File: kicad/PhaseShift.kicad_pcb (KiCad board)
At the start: 2 copper layers, 66.4 x 128.6 mm, 39 parts

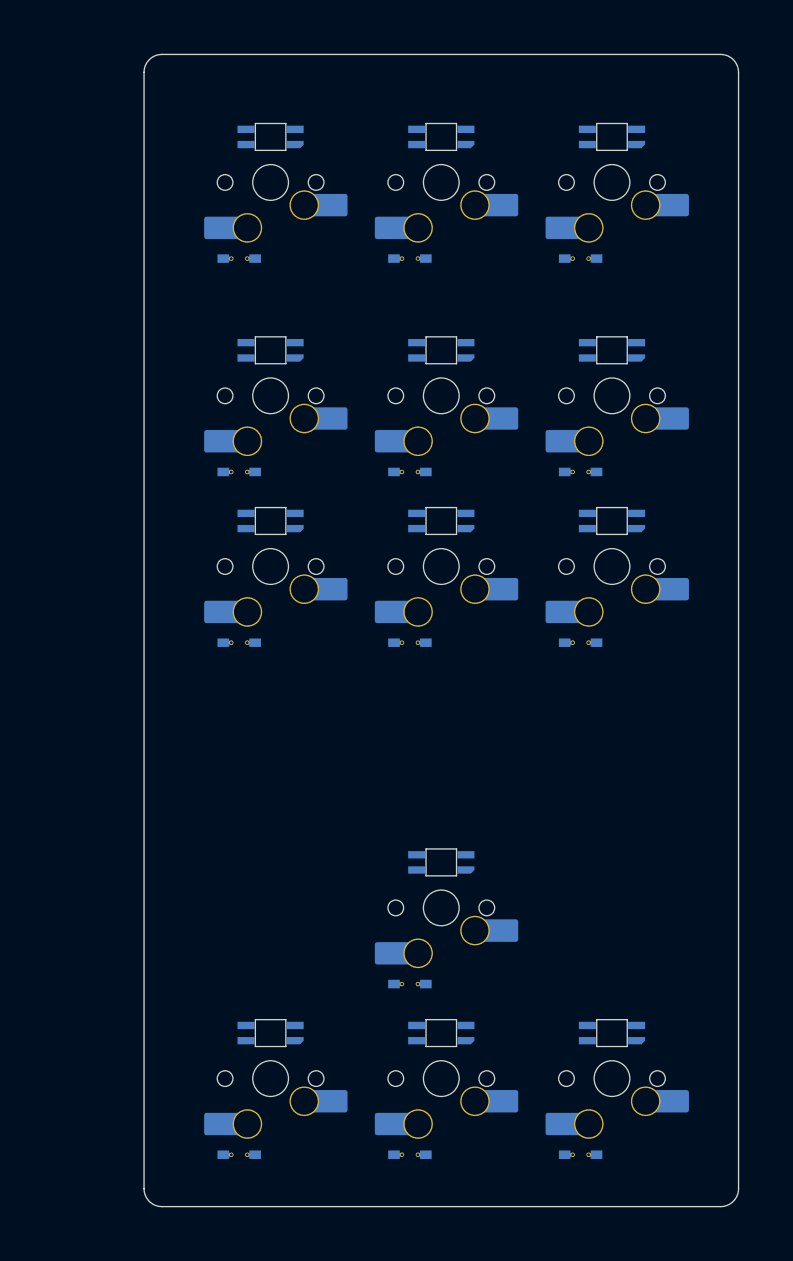
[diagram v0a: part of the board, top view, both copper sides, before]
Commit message: added MCU
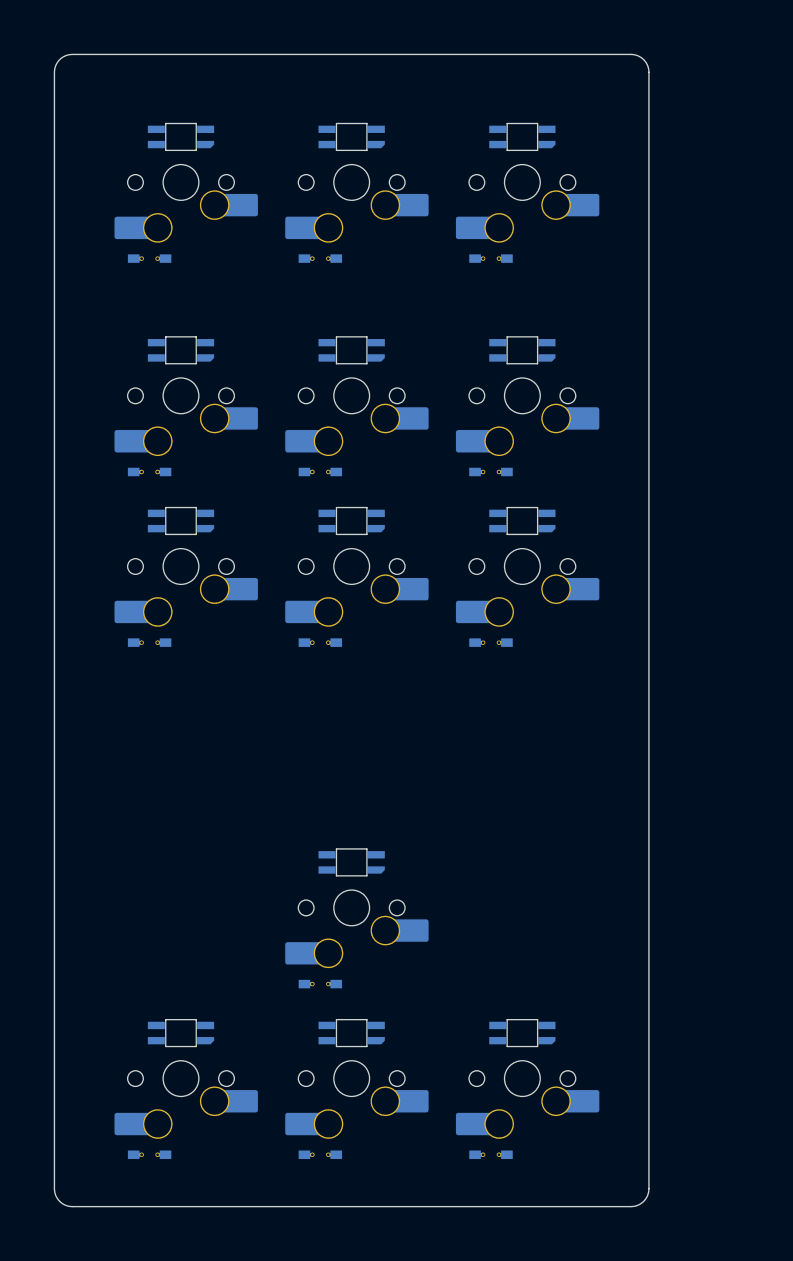
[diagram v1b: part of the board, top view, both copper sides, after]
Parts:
- moved D1 10.0 mm to (161.9, 98.5)
- moved D10 10.0 mm to (181.0, 179.5)
- moved D11 10.0 mm to (161.9, 198.5)
- moved D12 10.0 mm to (181.0, 198.5)
- moved D13 10.0 mm to (200.1, 198.5)
- moved D2 10.0 mm to (161.9, 122.3)
- moved D3 10.0 mm to (161.9, 141.4)
- moved D4 10.0 mm to (181.0, 98.5)
- moved D5 10.0 mm to (181.0, 122.3)
- moved D6 10.0 mm to (181.0, 141.4)
- moved D7 10.0 mm to (200.1, 98.5)
- moved D8 10.0 mm to (200.1, 122.3)
- moved D9 10.0 mm to (200.1, 141.4)
- moved L1 10.0 mm to (165.4, 84.9)
- moved L10 10.0 mm to (184.5, 165.9)
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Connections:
- S1 pad 1: col_0 -> Net-(D1-A)
- S1 pad 2: Net-(D1-A) -> col_0
- S10 pad 1: col_1 -> Net-(D10-A)
- S10 pad 2: Net-(D10-A) -> col_1
- S11 pad 1: col_0 -> Net-(D11-A)
- S11 pad 2: Net-(D11-A) -> col_0
- S12 pad 1: col_1 -> Net-(D12-A)
- S12 pad 2: Net-(D12-A) -> col_1
- S13 pad 1: col_2 -> Net-(D13-A)
- S13 pad 2: Net-(D13-A) -> col_2
- S2 pad 1: col_0 -> Net-(D2-A)
- S2 pad 2: Net-(D2-A) -> col_0
- S3 pad 1: col_0 -> Net-(D3-A)
- S3 pad 2: Net-(D3-A) -> col_0
- S4 pad 1: col_1 -> Net-(D4-A)
- S4 pad 2: Net-(D4-A) -> col_1
- S5 pad 1: col_1 -> Net-(D5-A)
- S5 pad 2: Net-(D5-A) -> col_1
- S6 pad 1: col_1 -> Net-(D6-A)
- S6 pad 2: Net-(D6-A) -> col_1
- S7 pad 1: col_2 -> Net-(D7-A)
- S7 pad 2: Net-(D7-A) -> col_2
- S8 pad 1: col_2 -> Net-(D8-A)
- S8 pad 2: Net-(D8-A) -> col_2
- S9 pad 1: col_2 -> Net-(D9-A)
- S9 pad 2: Net-(D9-A) -> col_2

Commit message: updated MCU
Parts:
- D1, D10, D11, D12, D13, D2, D3, D4, D5, D6, D7, D8, D9: value 1N4148W -> (none)
- S1, S10, S11, S12, S2, S3, S4, S5, S6, S7, S8, S9: value SW_MX_HS -> (none)
- S13: value SW_MX_HS_1u -> (none)
- moved D1 210.0 mm to (372.0, 98.5)
- moved D10 210.0 mm to (391.0, 179.5)
- moved D11 210.0 mm to (372.0, 198.5)
- moved D12 210.0 mm to (391.0, 198.5)
- moved D13 210.0 mm to (410.1, 198.5)
- moved D2 210.0 mm to (372.0, 122.3)
- moved D3 210.0 mm to (372.0, 141.4)
- moved D4 210.0 mm to (391.0, 98.5)
- moved D5 210.0 mm to (391.0, 122.3)
- moved D6 210.0 mm to (391.0, 141.4)
- moved D7 210.0 mm to (410.1, 98.5)
- moved D8 210.0 mm to (410.1, 122.3)
- moved D9 210.0 mm to (410.1, 141.4)
- moved L1 210.0 mm to (375.5, 84.9)
- moved L10 210.0 mm to (394.5, 165.9)
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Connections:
- net Net-(D1-A) renamed c14_func
- net Net-(D10-A) renamed c15_bottom
- net Net-(D11-A) renamed c14_thumb
- net Net-(D12-A) renamed c15_thumb
- net Net-(D13-A) renamed c16_thumb
- net Net-(D2-A) renamed c14_number
- net Net-(D3-A) renamed c14_top
- net Net-(D4-A) renamed c15_func
- net Net-(D5-A) renamed c15_number
- net Net-(D6-A) renamed c15_top
- net Net-(D7-A) renamed c16_func
- net Net-(D8-A) renamed c16_number
- net Net-(D9-A) renamed c16_top
- net col_2 renamed col_3
- net row_12 renamed function
- net row_13 renamed number
- net row_14 renamed top
- net row_16 renamed bottom
- net row_17 renamed thumb
- S1 pad 2: col_0 -> col_1
- S10 pad 2: col_1 -> col_4
- S11 pad 2: col_0 -> col_1
- S12 pad 2: col_1 -> col_4
- S2 pad 2: col_0 -> col_1
- S3 pad 2: col_0 -> col_1
- S4 pad 2: col_1 -> col_4
- S5 pad 2: col_1 -> col_4
- S6 pad 2: col_1 -> col_4

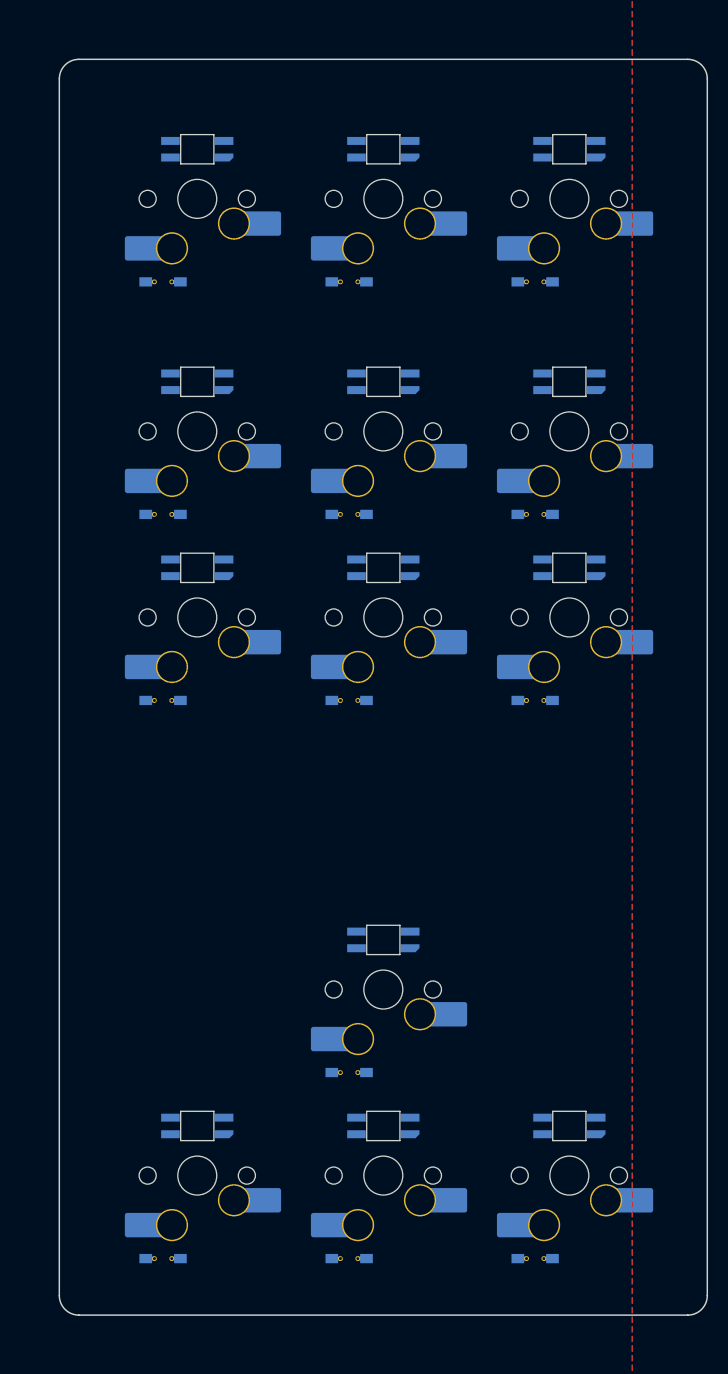
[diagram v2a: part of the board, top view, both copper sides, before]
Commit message: screw holes
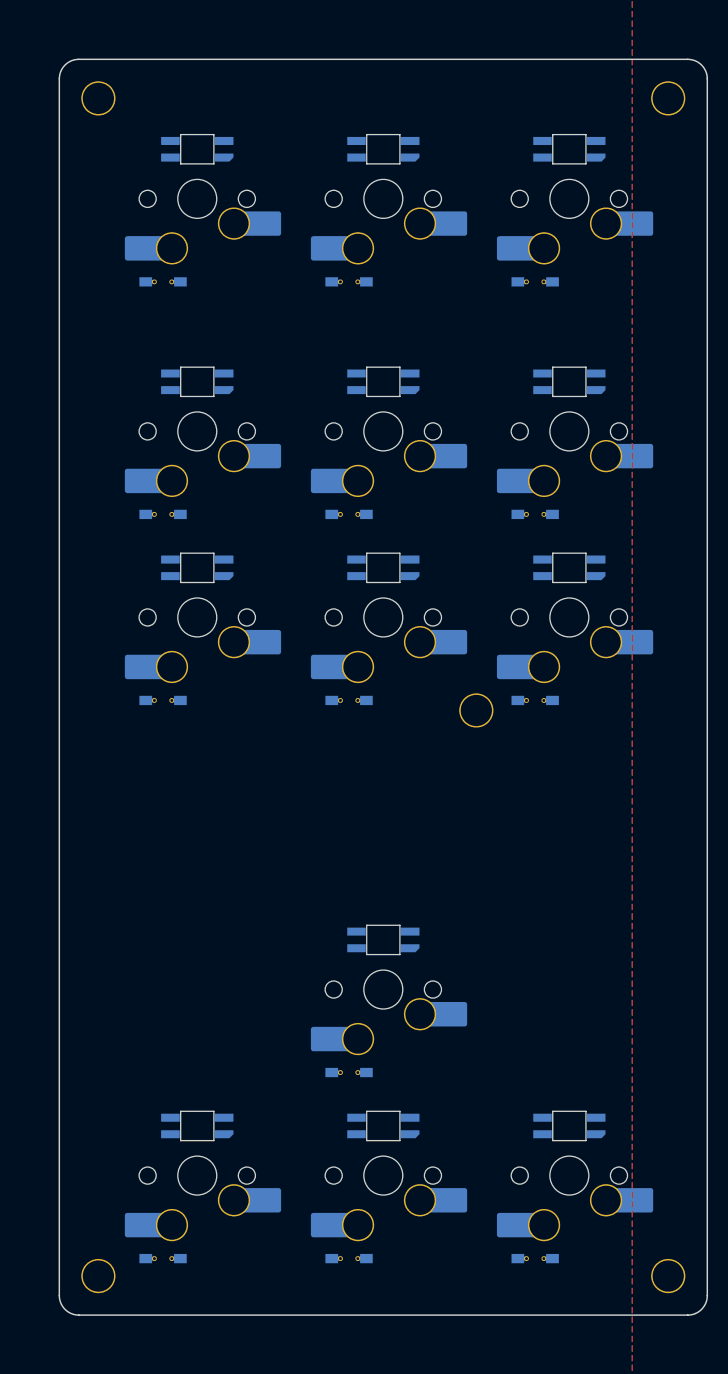
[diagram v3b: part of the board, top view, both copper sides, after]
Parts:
- added H1: MountingHole_3.2mm_Pad, TB2086_MISC:MountingHole_3.2mm_Pad, F.Cu at (365.3, 79.7)
- added H2: MountingHole_3.2mm_Pad, TB2086_MISC:MountingHole_3.2mm_Pad, F.Cu at (423.7, 79.7)
- added H3: MountingHole_3.2mm_Pad, TB2086_MISC:MountingHole_3.2mm_Pad, F.Cu at (423.7, 200.3)
- added H4: MountingHole_3.2mm_Pad, TB2086_MISC:MountingHole_3.2mm_Pad, F.Cu at (365.3, 200.3)
- added H5: MountingHole_3.2mm_Pad, TB2086_MISC:MountingHole_3.2mm_Pad, F.Cu at (404.0, 142.4)

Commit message: pogo pin - ergogen
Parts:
- added POGO1: Pogopin_1x05_P2.54mm_Curved, TB2086_MISC:Pogopin_1x05_P2.54mm_Curved, B.Cu at (175.4, 95.5)
- added POGO2: Pogopin_1x05_P2.54mm_Curved, TB2086_MISC:Pogopin_1x05_P2.54mm_Curved, B.Cu at (233.6, 95.5)
- added POGO3: Pogopin_1x07_P2.54mm_Curved, TB2086_MISC:Pogopin_1x07_P2.54mm_Curved, B.Cu at (175.4, 142.4)
- added POGO4: Pogopin_1x07_P2.54mm_Curved, TB2086_MISC:Pogopin_1x07_P2.54mm_Curved, B.Cu at (233.6, 142.4)
- added POGO5: Pogopin_1x07_P2.54mm_Curved, TB2086_MISC:Pogopin_1x07_P2.54mm_Curved, B.Cu at (175.4, 182.0)
- added POGO6: Pogopin_1x07_P2.54mm_Curved, TB2086_MISC:Pogopin_1x07_P2.54mm_Curved, B.Cu at (233.6, 182.0)
- moved D1 190.0 mm to (181.9, 98.5)
- moved D10 190.0 mm to (201.0, 179.5)
- moved D11 190.0 mm to (181.9, 198.5)
- moved D12 190.0 mm to (201.0, 198.5)
- moved D13 190.0 mm to (220.1, 198.5)
- moved D2 190.0 mm to (181.9, 122.3)
- moved D3 190.0 mm to (181.9, 141.4)
- moved D4 190.0 mm to (201.0, 98.5)
- moved D5 190.0 mm to (201.0, 122.3)
- moved D6 190.0 mm to (201.0, 141.4)
- moved D7 190.0 mm to (220.1, 98.5)
- moved D8 190.0 mm to (220.1, 122.3)
- moved D9 190.0 mm to (220.1, 141.4)
- moved H1 190.0 mm to (175.3, 79.7)
- moved H2 190.0 mm to (233.7, 79.7)
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
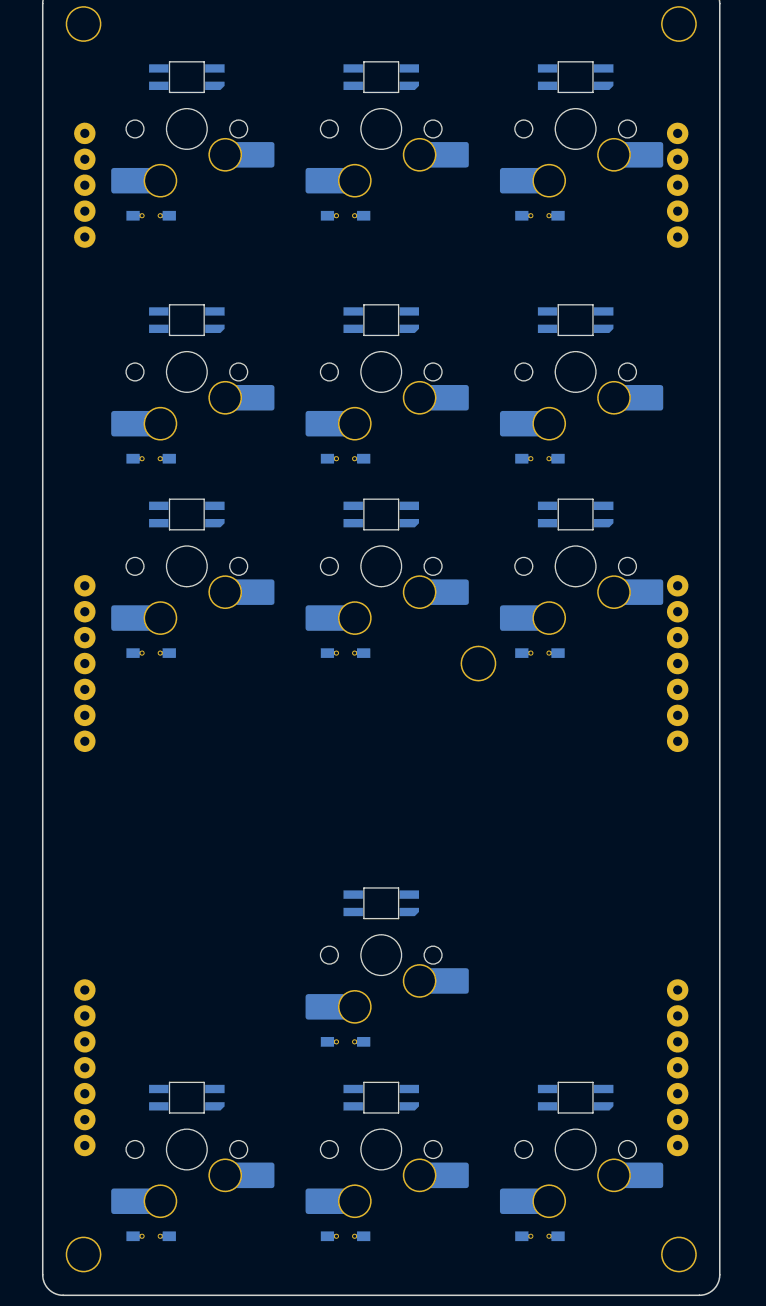
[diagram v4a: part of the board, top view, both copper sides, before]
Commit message: artwork for PhaseShift
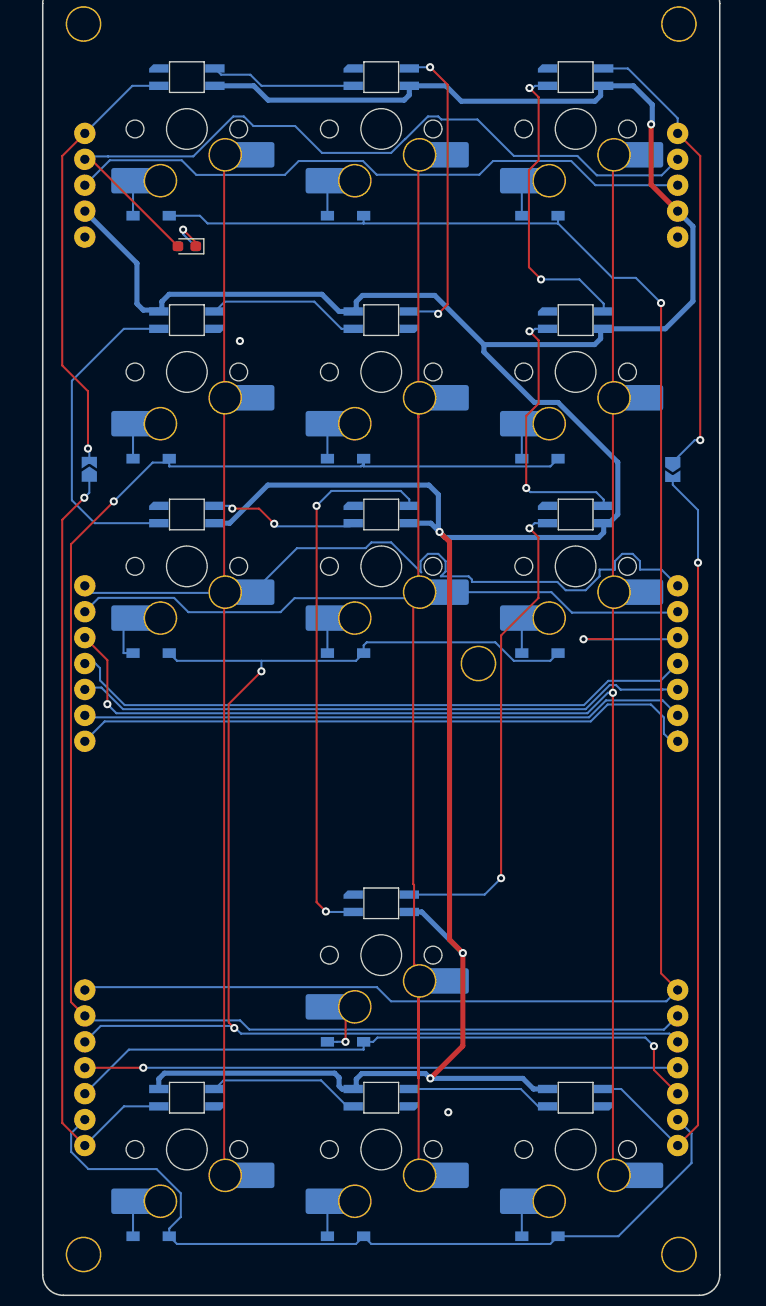
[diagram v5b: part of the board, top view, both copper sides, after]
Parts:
- added JP1: SolderJumper_2_Open, TB2086_MISC:SolderJumper-2_P1.3mm_Open_TrianglePad1.0x1.5mm, B.Cu at (175.9, 123.3)
- added JP2: SolderJumper_2_Open, TB2086_MISC:SolderJumper-2_P1.3mm_Open_TrianglePad1.0x1.5mm, B.Cu at (233.1, 123.4)
- added LED1: GREEN, LED_SMD:LED_0603_1608Metric_Pad1.05x0.95mm_HandSolder, F.Cu at (185.4, 101.5)
- added R1: 330, Resistor_SMD:R_0603_1608Metric, B.Cu at (185.4, 101.5)
- D1, D10, D11, D12, D13, D2, D3, D4, D5, D6, D7, D8, D9: value (none) -> 1N4148W
- L1, L10, L11, L12, L13, L2, L3, L4, L5, L6, L7, L8, L9: value TB2086_LED:LED_SK6812MINI-E -> SK6812MINI-E; footprint TB2086_LED:LED_SK6812MINI-E -> TB2086_LED_G:LED_SK6812MINI-E
- POGO1, POGO2: value Pogopin_1x05_P2.54mm_Curved -> Conn_01x05
- POGO3, POGO4, POGO5, POGO6: value Pogopin_1x07_P2.54mm_Curved -> Conn_01x07
- S1, S10, S11, S12, S2, S3, S4, S5, S6, S7, S8, S9: value (none) -> SW_MX_HS
- S13: value (none) -> SW_MX_HS_1u
- turned L1 to 180 degrees
- turned L10 to 180 degrees
- turned L3 to 180 degrees
- turned L4 to 180 degrees
- turned L6 to 180 degrees
- turned L7 to 180 degrees
- turned L8 to 180 degrees
- turned L9 to 180 degrees
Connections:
- net c14_func renamed Net-(D1-A)
- net c14_number renamed Net-(D2-A)
- net c14_thumb renamed Net-(D11-A)
- net c14_top renamed Net-(D3-A)
- net c15_bottom renamed Net-(D10-A)
- net c15_func renamed Net-(D4-A)
- net c15_number renamed Net-(D5-A)
- net c15_thumb renamed Net-(D12-A)
- net c15_top renamed Net-(D6-A)
- net c16_func renamed Net-(D7-A)
- net c16_number renamed Net-(D8-A)
- net c16_thumb renamed Net-(D13-A)
- net c16_top renamed Net-(D9-A)
- D1 pad 1: function -> ROW12
- D10 pad 1: bottom -> ROW16
- D11 pad 1: thumb -> ROW17
- D12 pad 1: thumb -> ROW17
- D13 pad 1: thumb -> ROW17
- D2 pad 1: number -> ROW13
- D3 pad 1: top -> ROW14
- D4 pad 1: function -> ROW12
- D5 pad 1: number -> ROW13
- D6 pad 1: top -> ROW14
- D7 pad 1: function -> ROW12
- D8 pad 1: number -> ROW13
- D9 pad 1: top -> ROW14
- L1 pad 1: VCC -> +5V
- L1 pad 2: (no net) -> Net-(L1-DOUT)
- L1 pad 4: (no net) -> RGB_FOM_LEFT
- L10 pad 1: VCC -> +5V
- L10 pad 2: (no net) -> Net-(L10-DOUT)
- L10 pad 4: (no net) -> Net-(L10-DIN)
- L11 pad 1: VCC -> +5V
- L11 pad 2: (no net) -> RGB_TO_LEFT
- L11 pad 4: (no net) -> Net-(L11-DIN)
- L12 pad 1: VCC -> +5V
- L12 pad 2: (no net) -> Net-(L11-DIN)
- L12 pad 4: (no net) -> Net-(L12-DIN)
- L13 pad 1: VCC -> +5V
- L13 pad 2: (no net) -> Net-(L12-DIN)
- L13 pad 4: (no net) -> RGB_FOM_RIGHT
- L2 pad 1: VCC -> +5V
- L2 pad 2: (no net) -> Net-(L2-DOUT)
- L2 pad 4: (no net) -> Net-(L2-DIN)
- L3 pad 1: VCC -> +5V
- L3 pad 2: (no net) -> Net-(L3-DOUT)
- L3 pad 4: (no net) -> Net-(L2-DOUT)
- L4 pad 1: VCC -> +5V
- L4 pad 2: (no net) -> Net-(L4-DOUT)
- L4 pad 4: (no net) -> Net-(L1-DOUT)
- L5 pad 1: VCC -> +5V
- L5 pad 2: (no net) -> Net-(L2-DIN)
- L5 pad 4: (no net) -> Net-(L4-DOUT)
- L6 pad 1: VCC -> +5V
- L6 pad 2: (no net) -> Net-(L10-DIN)
- L6 pad 4: (no net) -> Net-(L3-DOUT)
- L7 pad 1: VCC -> +5V
- L7 pad 2: (no net) -> RGB_TO_RIGHT
- L7 pad 4: (no net) -> Net-(L7-DIN)
- L8 pad 1: VCC -> +5V
- L8 pad 2: (no net) -> Net-(L7-DIN)
- L8 pad 4: (no net) -> Net-(L8-DIN)
- L9 pad 1: VCC -> +5V
- L9 pad 2: (no net) -> Net-(L8-DIN)
- L9 pad 4: (no net) -> Net-(L10-DOUT)
- POGO1 pad 1: P1 -> RGB_FOM_LEFT
- POGO1 pad 2: P2 -> SCR
- POGO1 pad 3: P3 -> NUM
- POGO1 pad 4: P4 -> +5V
- POGO1 pad 5: P5 -> GND
- POGO2 pad 1: P1 -> GND
- POGO2 pad 2: P2 -> +5V
- POGO2 pad 3: P3 -> NUM
- POGO2 pad 4: P4 -> SCR
- POGO2 pad 5: P5 -> RGB_TO_RIGHT
- POGO3 pad 1: P1 -> COL0
- POGO3 pad 2: P2 -> COL1
- POGO3 pad 3: P3 -> COL2
- POGO3 pad 4: P4 -> COL3
- POGO3 pad 5: P5 -> COL4
- POGO3 pad 6: P6 -> COL5
- POGO3 pad 7: P7 -> COL6
- POGO4 pad 1: P1 -> COL6
- POGO4 pad 2: P2 -> COL5
- POGO4 pad 3: P3 -> COL4
- POGO4 pad 4: P4 -> COL3
- POGO4 pad 5: P5 -> COL2
- POGO4 pad 6: P6 -> COL1
- POGO4 pad 7: P7 -> COL0
- POGO5 pad 1: P1 -> ROW12
- POGO5 pad 2: P2 -> ROW13
- POGO5 pad 3: P3 -> ROW14
- POGO5 pad 4: P4 -> ROW15
- POGO5 pad 5: P5 -> ROW16
- POGO5 pad 6: P6 -> ROW17
- POGO5 pad 7: P7 -> RGB_TO_LEFT
- POGO6 pad 1: P1 -> RGB_FOM_RIGHT
- POGO6 pad 2: P2 -> ROW17
- POGO6 pad 3: P3 -> ROW16
- POGO6 pad 4: P4 -> ROW15
- POGO6 pad 5: P5 -> ROW14
- POGO6 pad 6: P6 -> ROW13
- POGO6 pad 7: P7 -> ROW12
- S1 pad 2: col_1 -> COL0
- S10 pad 2: col_4 -> COL1
- S11 pad 2: col_1 -> COL0
- S12 pad 2: col_4 -> COL1
- S13 pad 2: col_3 -> COL2
- S2 pad 2: col_1 -> COL0
- S3 pad 2: col_1 -> COL0
- S4 pad 2: col_4 -> COL1
- S5 pad 2: col_4 -> COL1
- S6 pad 2: col_4 -> COL1
- S7 pad 2: col_3 -> COL2
- S8 pad 2: col_3 -> COL2
- S9 pad 2: col_3 -> COL2
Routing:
- net +5V: track 0.00 -> 318.8 mm, vias 0 -> 4
- net COL2: track 0.00 -> 181.8 mm, vias 0 -> 3
- net COL1: track 0.00 -> 181.3 mm
- net ROW12: track 0.00 -> 180.1 mm, vias 0 -> 1
- net COL0: track 0.00 -> 177.9 mm
- net ROW13: track 0.00 -> 159.0 mm, vias 0 -> 1
- net ROW14: track 0.00 -> 137.1 mm, vias 0 -> 2
- net ROW17: track 0.00 -> 81.1 mm
- net SCR: track 0.00 -> 77.6 mm
- net RGB_FOM_RIGHT: track 0.00 -> 76.9 mm, vias 0 -> 1
- net RGB_TO_LEFT: track 0.00 -> 76.4 mm, vias 0 -> 1
- net ROW16: track 0.00 -> 64.0 mm, vias 0 -> 1
- net COL6: track 0.00 -> 63.3 mm
- net NUM: track 0.00 -> 62.4 mm
- net COL3: track 0.00 -> 61.3 mm
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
